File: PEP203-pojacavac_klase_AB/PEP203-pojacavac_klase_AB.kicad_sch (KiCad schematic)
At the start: 18 parts, among them J1 Screw_Terminal_01x02, J2 Conn_01x02_Pin, J3 Conn_01x02_Pin, J4 Conn_01x02_Pin, J5 Conn_01x02_Pin, Q1 MMBT2222A

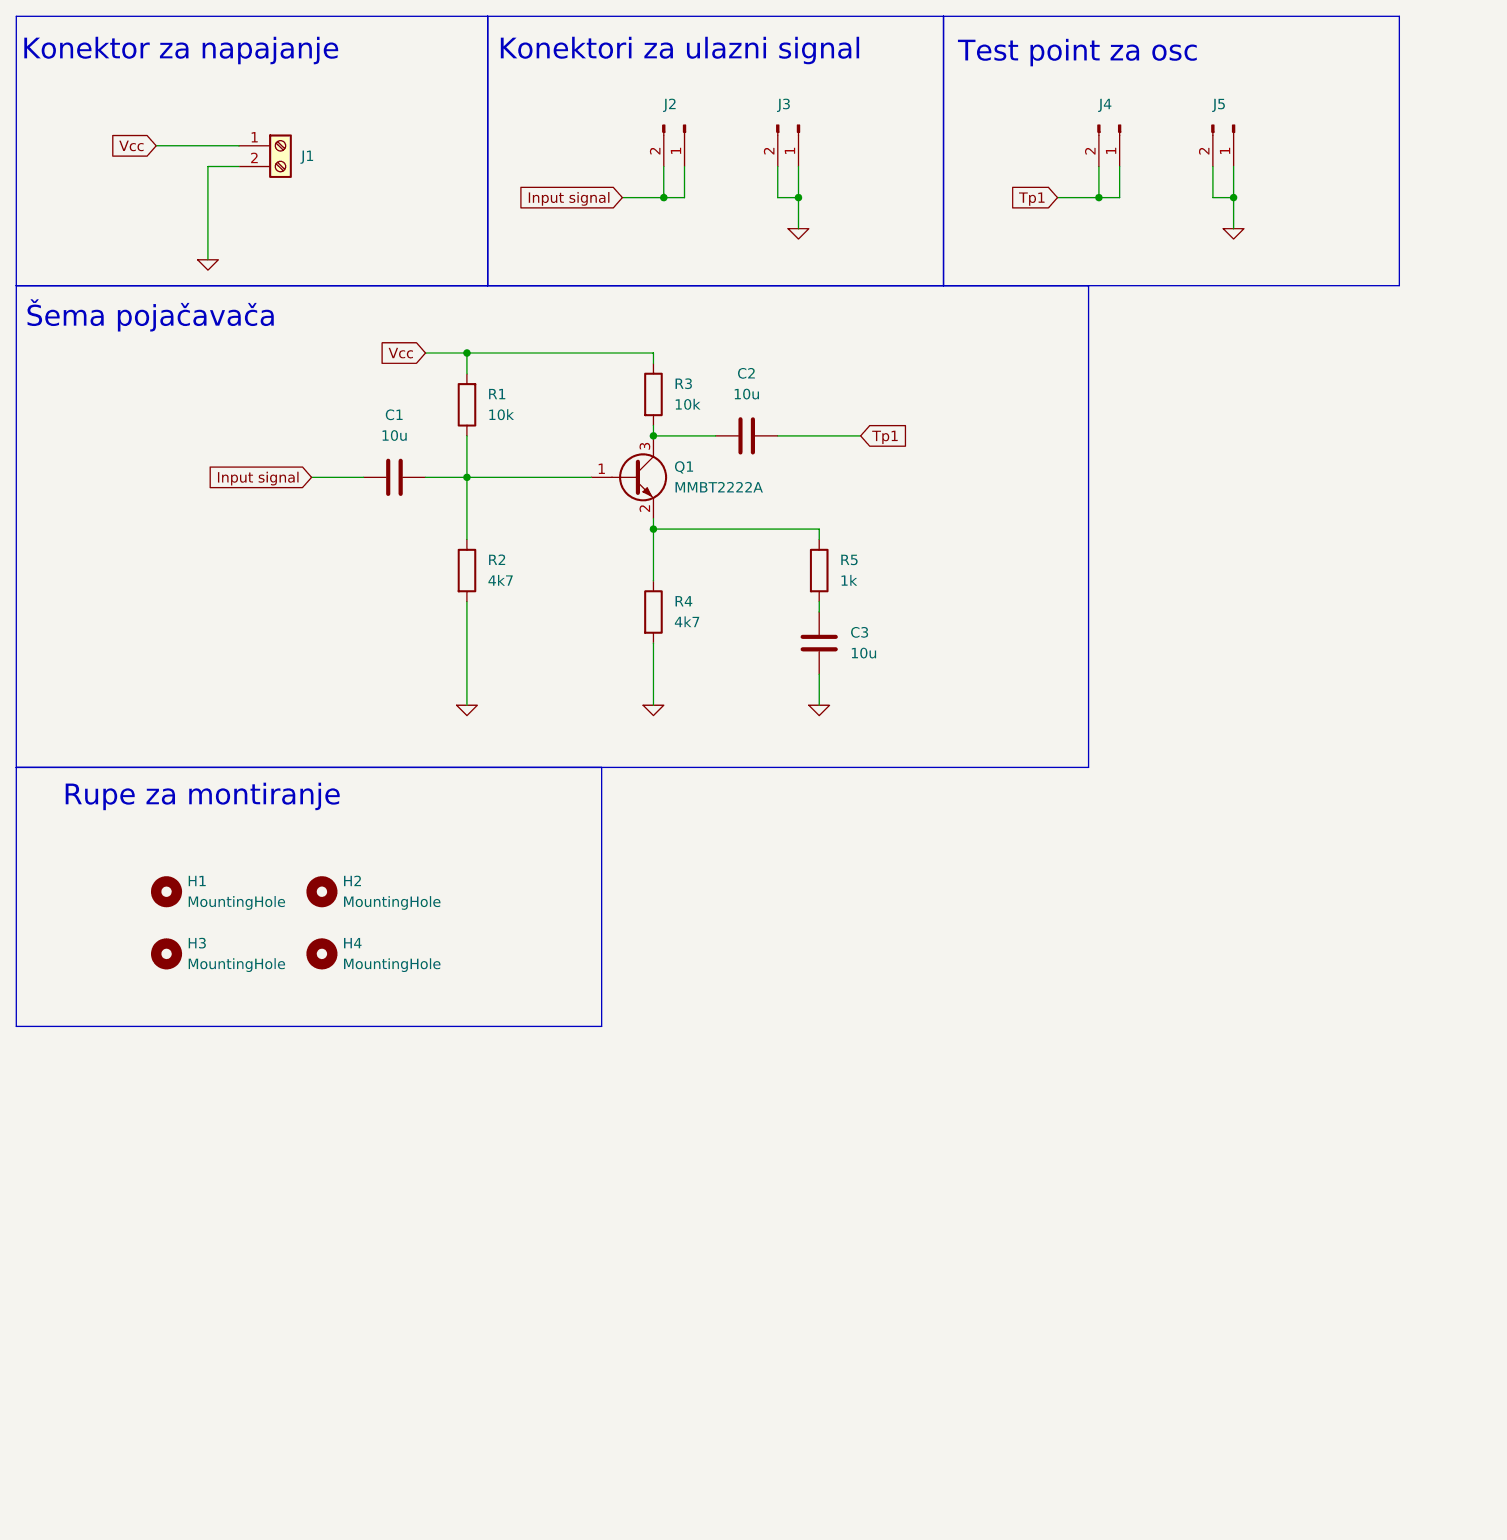
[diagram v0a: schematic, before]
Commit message: Sredjena estetika simulacije, dodati komentari.
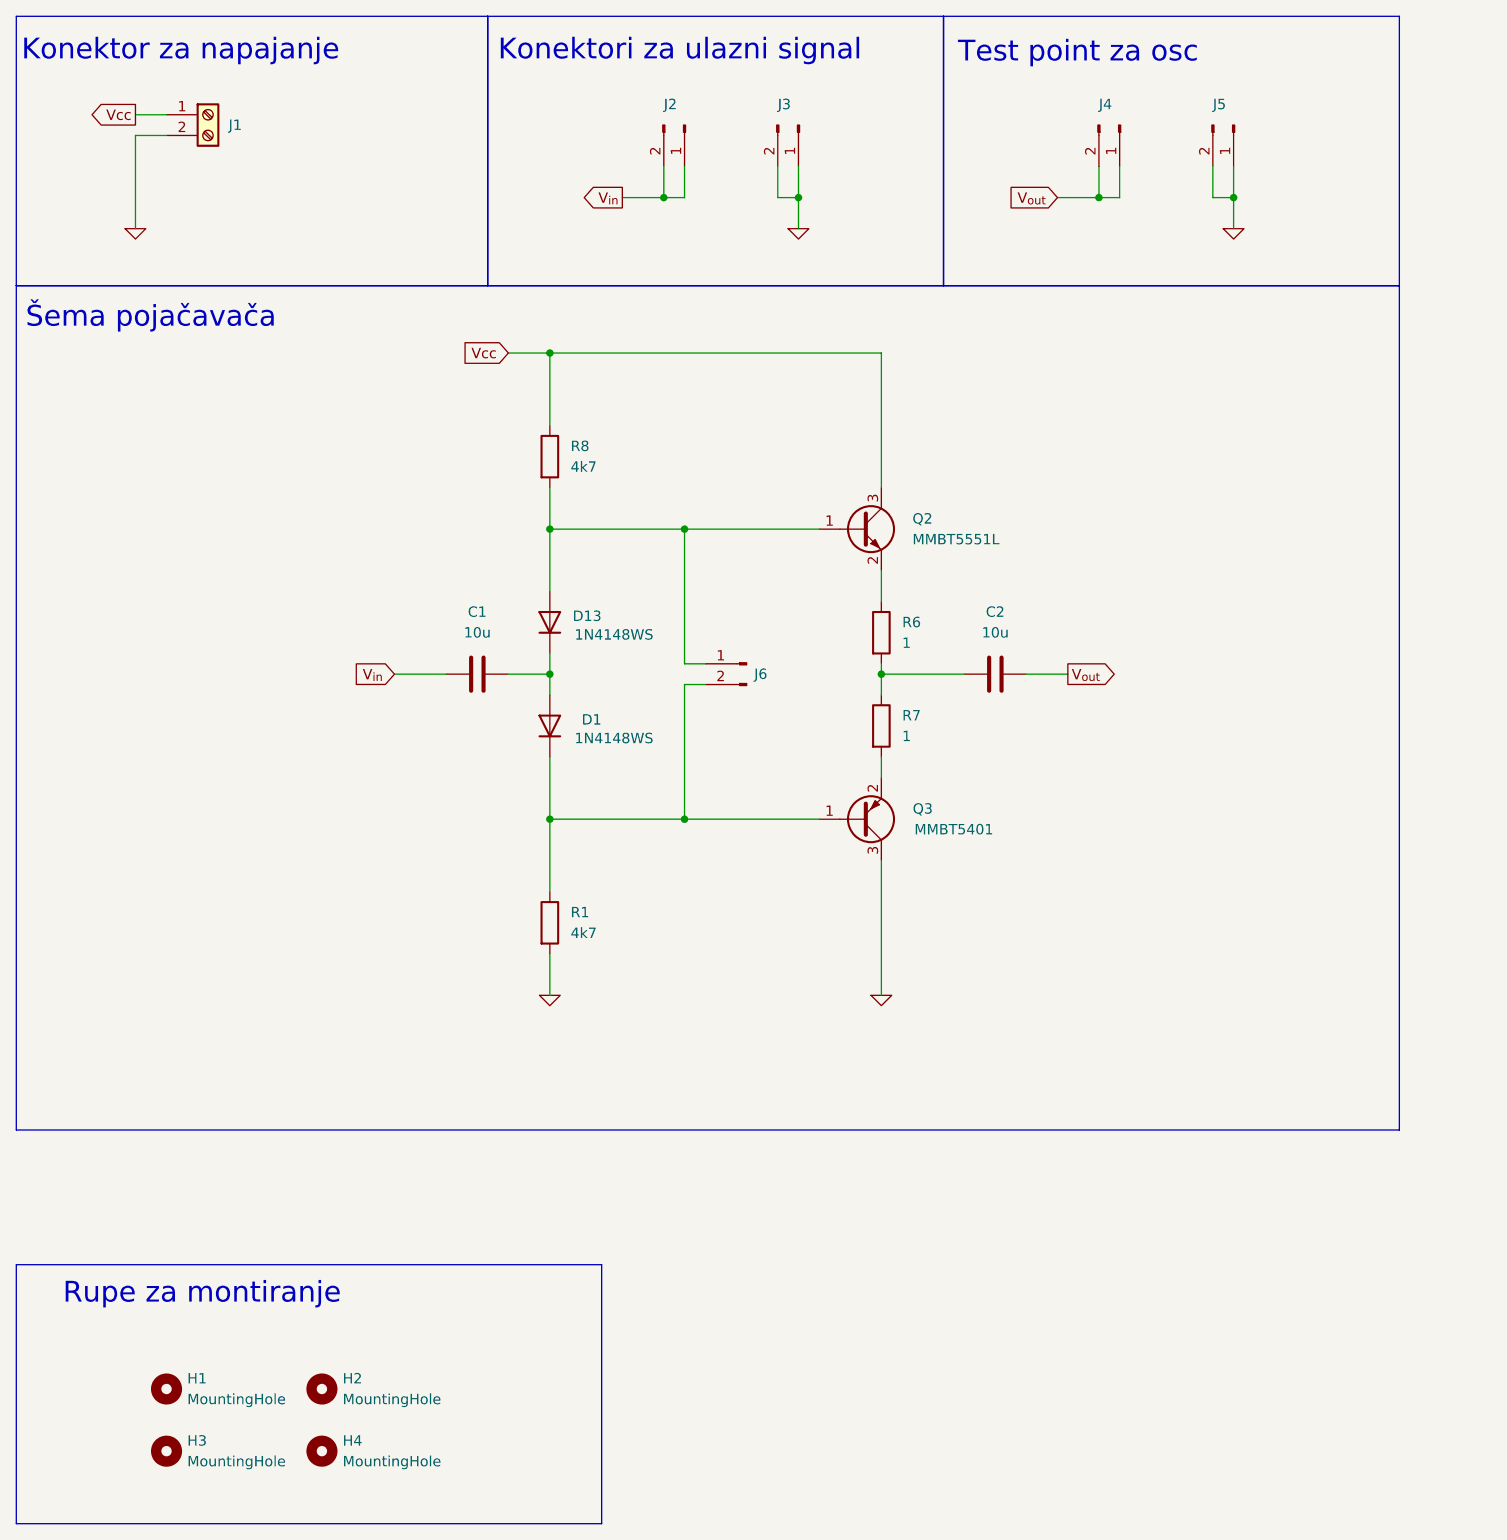
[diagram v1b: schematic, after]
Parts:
- removed C3: 10u, Capacitor_SMD:C_1206_3216Metric_Pad1.33x1.80mm_HandSolder, symbol Device:C
- removed Q1: MMBT2222A, Package_TO_SOT_SMD:SOT-23, symbol Transistor_BJT:MMBT2222A
- removed R2, R4: 4k7, Resistor_SMD:R_1206_3216Metric_Pad1.30x1.75mm_HandSolder, symbol PEP_library:R_SMD
- removed R3: 10k, Resistor_SMD:R_1206_3216Metric_Pad1.30x1.75mm_HandSolder, symbol PEP_library:R_SMD
- removed R5: 1k, Resistor_SMD:R_1206_3216Metric_Pad1.30x1.75mm_HandSolder, symbol PEP_library:R_SMD
- added D1, D13: 1N4148WS, Diode_SMD:D_SOD-323, symbol Diode:1N4148WS
- added J6: Conn_01x02_Pin, Connector_PinHeader_2.54mm:PinHeader_1x02_P2.54mm_Vertical, symbol Connector:Conn_01x02_Pin
- added Q2: MMBT5551L, Package_TO_SOT_SMD:SOT-23, symbol Transistor_BJT:MMBT5551L
- added Q3: MMBT5401, Package_TO_SOT_SMD:SOT-23, symbol Transistor_BJT:MMBT3906
- added R6, R7: 1, Resistor_SMD:R_1206_3216Metric_Pad1.30x1.75mm_HandSolder, symbol PEP_library:R_SMD
- added R8: 4k7, Resistor_SMD:R_1206_3216Metric_Pad1.30x1.75mm_HandSolder, symbol PEP_library:R_SMD
- R1: value 10k -> 4k7; LCSC C17902 -> C17936
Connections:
- net 0: now also R1.2, Q3.3 (C)
- net Vcc: now also Q2.3 (C), R8.1; no longer R1.2
- net at C2.1: now also R6.2, R7.1
- net at R1.1: now also D1.1 (K), J6.2 (Pin_2), Q3.1 (B); no longer C1.2
- net Input signal renamed V_{in}
- net Tp1 renamed V_{out}
- new net: Q2.2 (E), R6.1
- new net: D13.2 (A), J6.1 (Pin_1), Q2.1 (B), R8.2
- new net: Q3.2 (E), R7.2
- new net: C1.2, D1.2 (A), D13.1 (K)
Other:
- moved on the sheet: C1, H1, H2, H3, H4, J1

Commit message: Added class AB.
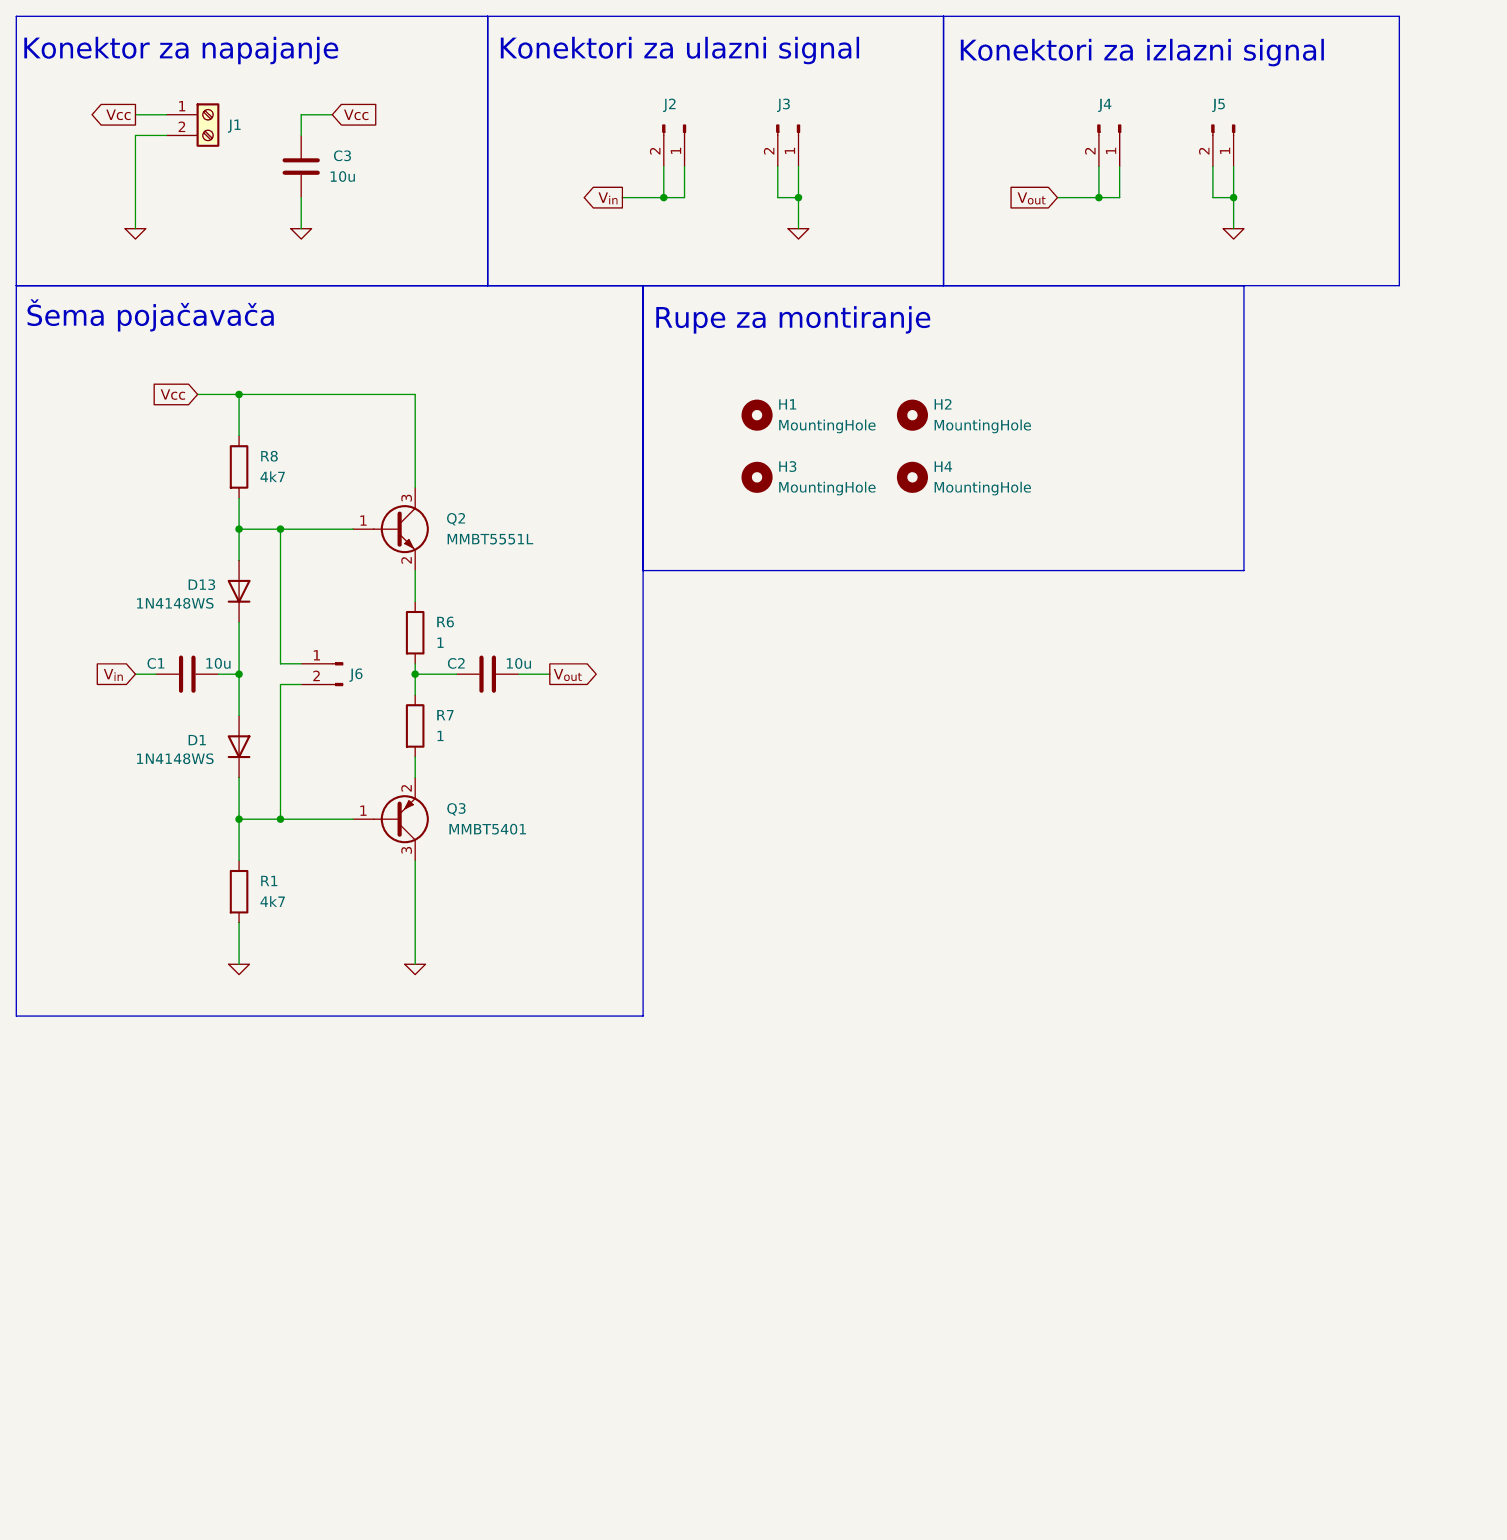
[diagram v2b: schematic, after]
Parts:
- added C3: 10u, Capacitor_SMD:C_1206_3216Metric_Pad1.33x1.80mm_HandSolder, symbol Device:C
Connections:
- net 0: now also C3.2
- net Vcc: now also C3.1
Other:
- note added: "Konektori za izlazni signal"
- note removed: "Test point za osc"
- moved on the sheet: C1, C2, D1, D13, H1, H2, H3, H4, J6, Q2, Q3, R1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
